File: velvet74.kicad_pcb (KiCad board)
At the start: 4 copper layers, 268 x 133.2 mm, 415 parts, among them J1 Connector, USB-TYPE-C-16P, J2 Connector, USB-TYPE-C-16P, J201 Connector, USB-TYPE-C-16P, J202 Connector, USB-TYPE-C-16P, J203 OLED 128x32, J3 OLED 128x32, SW1 BOOT, SW10 F0, SW11 F1, SW12 F2, SW13 F3, SW14 F4, SW15 F5, SW16 F6 Choc/EC11, SW2 RESET, SW20 N0, SW201 BOOT, SW202 RESET, SW21 N1, SW210 F0, SW211 F1, SW212 F2, SW213 F3, SW214 F4, SW215 F5, SW216 F6 Choc/EC11, SW22 N2, SW220 N0, SW221 N1, SW222 N2, SW223 N3, SW224 N4, SW225 N5, SW23 N3, SW230 T0, SW231 T1, SW232 T2, SW233 T3, SW234 T4, SW235 T5, SW24 N4, SW240 H0, SW241 H1, SW242 H2, SW243 H3, SW244 H4, SW245 H5, SW25 N5, SW250 B0, SW251 B1, SW252 B2, SW253 B3, SW254 B4, SW255 B5, SW260 TH0, SW261 TH1, SW262 TH2, SW263 TH3, SW264 TH4, SW265 TH5 Choc/EC11, SW30 T0, SW31 T1, SW32 T2, SW33 T3, SW34 T4, SW35 T5, SW40 H0, SW41 H1, SW42 H2, SW43 H3, SW44 H4, SW45 H5, SW50 B0, SW51 B1, SW52 B2, SW53 B3, SW54 B4, SW55 B5, SW60 TH0, SW61 TH1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

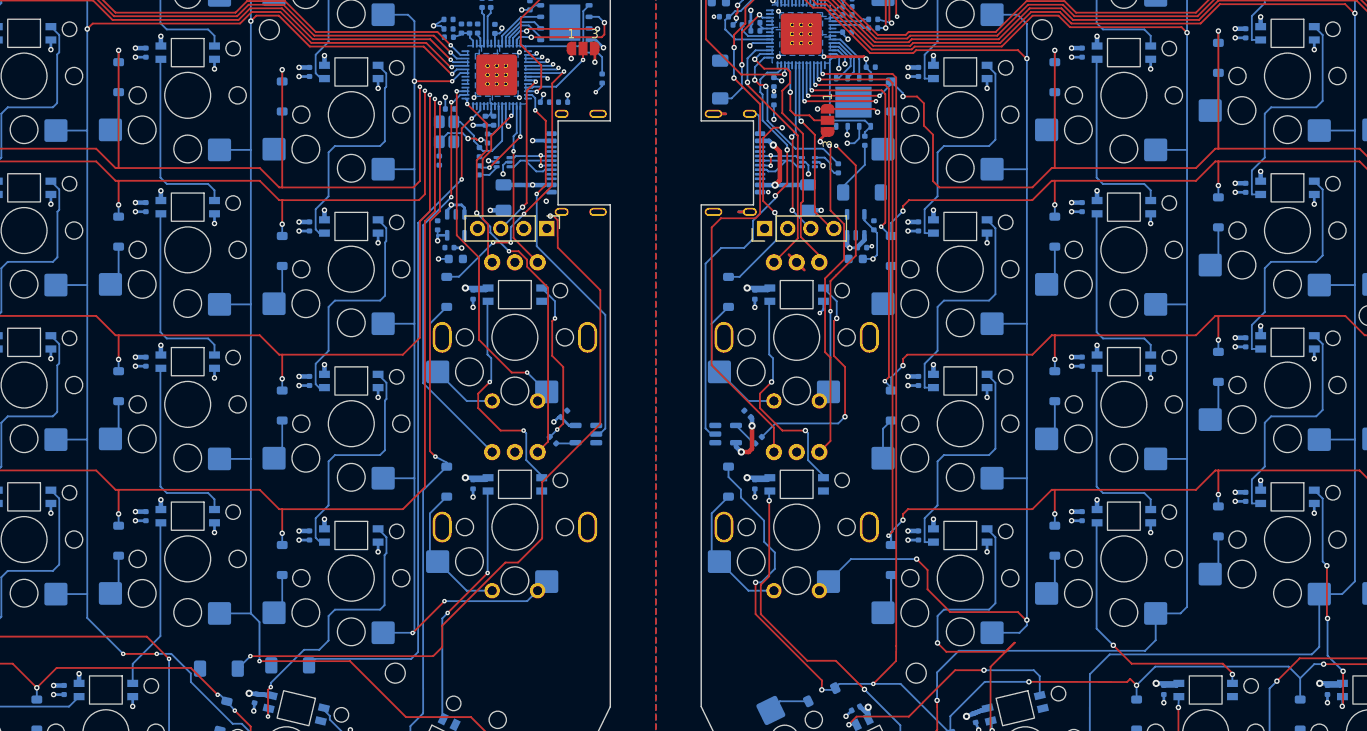
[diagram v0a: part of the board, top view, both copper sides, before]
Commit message: feat(pcb): move boot and reset together into spot c
BOOT and RESET now sit side by side, turned upright, at the same spot
on both halves (mirrored), so one opening in the case floor reaches
both buttons on either side.

- SW1/SW2 and SW201/SW202 placed by Ergogen mount points, with a
  button_boot/button_reset pair and a _button_hole cut in the case floor
- Left GP26 and right GP26 moved out of the new spot; RUN and the BOOT
  resistor nets re-routed to the new buttons on both halves
- Both production sets and the left prototype case and PCB dummy
  regenerated

Under the hood: the right RUN (20 segments, 9 vias, one In1 run) and
BOOT (10 segments, 4 vias) routes are autorouted and may want a hand
pass.

Checks: ERC 0; DRC 42 known items, 0 unconnected, 0 parity; jumper pad
groups 4; gerber connectivity shows no opens and only the USBLC6 pad
links.
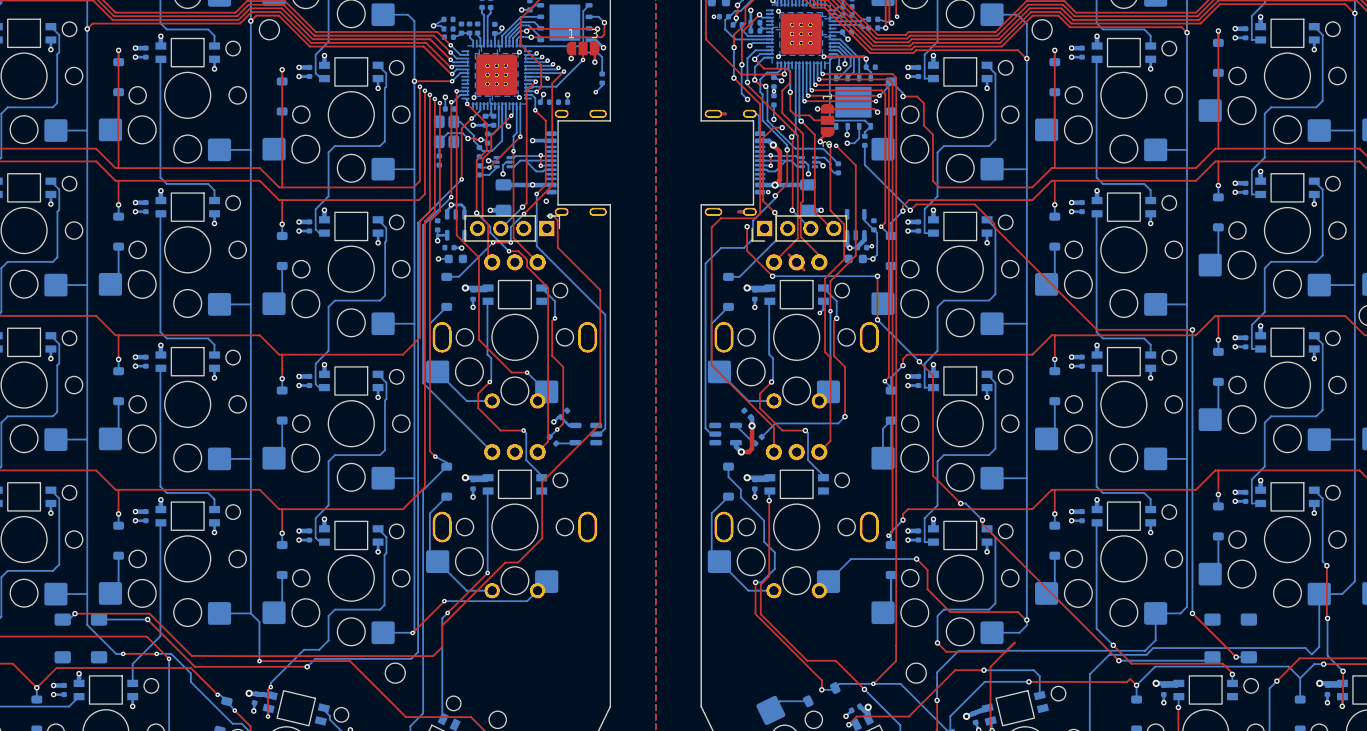
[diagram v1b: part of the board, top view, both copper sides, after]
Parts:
- moved SW202 81.9 mm to (244.8, 146.0)
- moved SW201 65.0 mm to (248.8, 146.0), turned to -90 degrees
- moved SW2 21.2 mm to (122.2, 146.0), turned to 90 degrees
- moved SW1 17.5 mm to (118.2, 146.0), turned to 90 degrees
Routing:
- net /Right/RUN: track 13.0 -> 109.2 mm, vias 2 -> 11
- net Net-(R204-Pad1): track 6.17 -> 85.8 mm, vias 0 -> 4
- net /Left/RUN: track 75.5 -> 100.8 mm, vias 2 -> 4
- net Net-(R4-Pad1): track 100.8 -> 121.3 mm
- net /Right/GP26: track 200.2 -> 200.8 mm
